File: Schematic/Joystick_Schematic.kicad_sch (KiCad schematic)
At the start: 4 parts

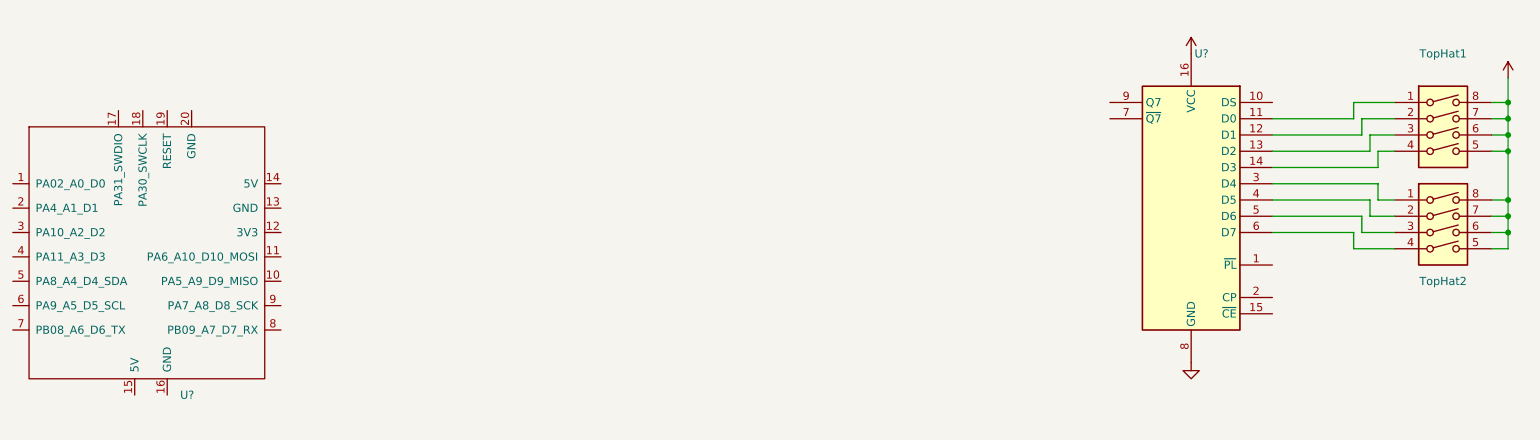
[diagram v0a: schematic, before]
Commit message: removed out of date files and created prove of concept piso code
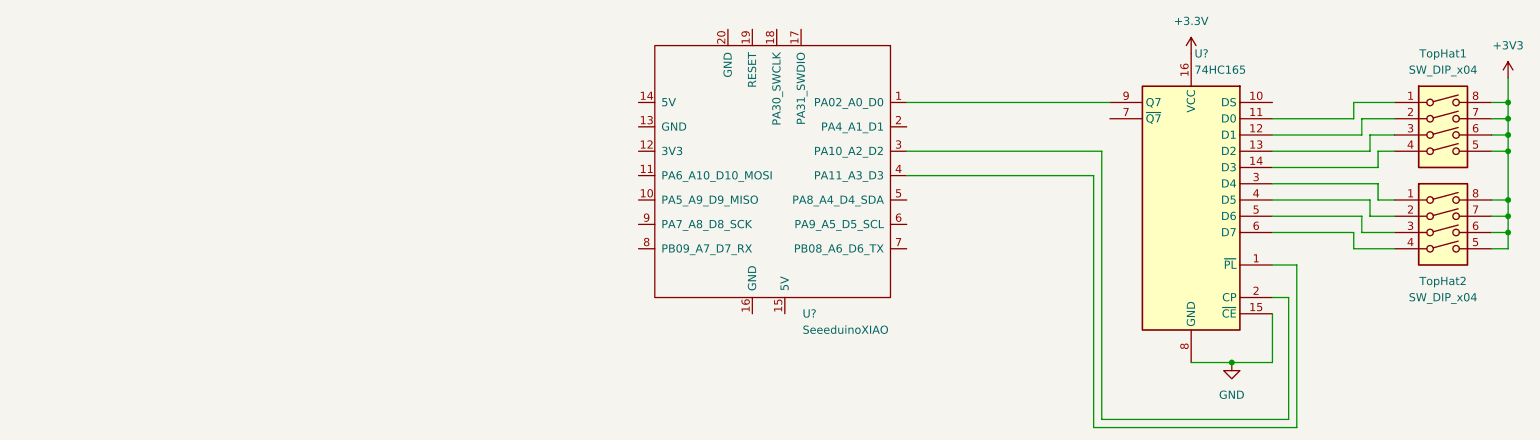
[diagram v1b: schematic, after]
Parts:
- TopHat1, TopHat2: value (none) -> SW_DIP_x04
- U?: value (none) -> SeeeduinoXIAO
- U?: value (none) -> 74HC165
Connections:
- net GND: now also U?.15 (~{CE})
- net at U?.1 (PA02_A0_D0): now also U?.9 (Q7)
- net at U?.3 (PA10_A2_D2): now also U?.2 (CP)
- net at U?.4 (PA11_A3_D3): now also U?.1 (~{PL})
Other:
- moved on the sheet: U?
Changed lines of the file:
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@@
   (junction (at 281.94 40.64) (diameter 0) (color 0 0 0 0)
   )
+  (junction (at 238.76 78.74) (diameter 0) (color 0 0 0 0)
+  )
   (junction (at 281.94 43.18) (diameter 0) (color 0 0 0 0)
   )
+  (wire (pts (xy 217.17 88.9) (xy 217.17 49.53))
+    (stroke (width 0) (type default) (color 0 0 0 0))
+  )
   (wire (pts (xy 257.81 38.1) (xy 257.81 40.64))
     (stroke (width 0) (type default) (color 0 0 0 0))
   )
+  (wire (pts (xy 248.92 63.5) (xy 245.11 63.5))
+    (stroke (width 0) (type default) (color 0 0 0 0))
+  )
   (wire (pts (xy 279.4 43.18) (xy 281.94 43.18))
     (stroke (width 0) (type default) (color 0 0 0 0))
@@
     (stroke (width 0) (type default) (color 0 0 0 0))
   )
+  (wire (pts (xy 247.65 68.58) (xy 247.65 87.63))
+    (stroke (width 0) (type default) (color 0 0 0 0))
+  )
+  (wire (pts (xy 217.17 88.9) (xy 248.92 88.9))
+    (stroke (width 0) (type default) (color 0 0 0 0))
+  )
+  (wire (pts (xy 245.11 78.74) (xy 245.11 71.12))
+    (stroke (width 0) (type default) (color 0 0 0 0))
+  )
   (wire (pts (xy 281.94 38.1) (xy 279.4 38.1))
     (stroke (width 0) (type default) (color 0 0 0 0))
@@
     (stroke (width 0) (type default) (color 0 0 0 0))
   )
+  (wire (pts (xy 218.44 45.72) (xy 187.96 45.72))
+    (stroke (width 0) (type default) (color 0 0 0 0))
+  )
   (wire (pts (xy 260.35 55.88) (xy 260.35 53.34))
     (stroke (width 0) (type default) (color 0 0 0 0))
@@
     (stroke (width 0) (type default) (color 0 0 0 0))
   )
+  (wire (pts (xy 218.44 87.63) (xy 218.44 45.72))
+    (stroke (width 0) (type default) (color 0 0 0 0))
+  )
   (wire (pts (xy 279.4 58.42) (xy 281.94 58.42))
     (stroke (width 0) (type default) (color 0 0 0 0))
   )
+  (wire (pts (xy 238.76 78.74) (xy 245.11 78.74))
+    (stroke (width 0) (type default) (color 0 0 0 0))
+  )
+  (wire (pts (xy 245.11 68.58) (xy 247.65 68.58))
+    (stroke (width 0) (type default) (color 0 0 0 0))
+  )
   (wire (pts (xy 259.08 40.64) (xy 259.08 43.18))
     (stroke (width 0) (type default) (color 0 0 0 0))
@@
     (stroke (width 0) (type default) (color 0 0 0 0))
   )
+  (wire (pts (xy 217.17 49.53) (xy 187.96 49.53))
+    (stroke (width 0) (type default) (color 0 0 0 0))
+  )
   (wire (pts (xy 257.81 60.96) (xy 257.81 58.42))
     (stroke (width 0) (type default) (color 0 0 0 0))
@@
     (stroke (width 0) (type default) (color 0 0 0 0))
   )
+  (wire (pts (xy 187.96 38.1) (xy 219.71 38.1))
+    (stroke (width 0) (type default) (color 0 0 0 0))
+  )
   (wire (pts (xy 259.08 55.88) (xy 259.08 58.42))
     (stroke (width 0) (type default) (color 0 0 0 0))
@@
     (stroke (width 0) (type default) (color 0 0 0 0))
   )
+  (wire (pts (xy 247.65 87.63) (xy 218.44 87.63))
+    (stroke (width 0) (type default) (color 0 0 0 0))
+  )
   (wire (pts (xy 261.62 45.72) (xy 261.62 48.26))
     (stroke (width 0) (type default) (color 0 0 0 0))
@@
     (stroke (width 0) (type default) (color 0 0 0 0))
   )
+  (wire (pts (xy 248.92 88.9) (xy 248.92 63.5))
+    (stroke (width 0) (type default) (color 0 0 0 0))
+  )
   (wire (pts (xy 279.4 40.64) (xy 281.94 40.64))
     (stroke (width 0) (type default) (color 0 0 0 0))
@@
     (stroke (width 0) (type default) (color 0 0 0 0))
   )
+  (wire (pts (xy 238.76 78.74) (xy 232.41 78.74))
+    (stroke (width 0) (type default) (color 0 0 0 0))
+  )
   (wire (pts (xy 279.4 60.96) (xy 281.94 60.96))
     (stroke (width 0) (type default) (color 0 0 0 0))
@@
     (stroke (width 0) (type default) (color 0 0 0 0))
   )
-  (symbol (lib_id "power:GND") (at 232.41 78.74 0) (unit 1)
-    (in_bom yes) (on_board yes) (fields_autoplaced)
-    (property "Reference" "#PWR?" (id 0) (at 232.41 85.09 0)
-      (effects (font (size 1.27 1.27)) hide)
-    )
-    (property "Value" "" (id 1) (at 232.41 83.82 0))
-    (property "Footprint" "" (id 2) (at 232.41 78.74 0)
-      (effects (font (size 1.27 1.27)) hide)
-    )
-    (property "Datasheet" "" (id 3) (at 232.41 78.74 0)
-      (effects (font (size 1.27 1.27)) hide)
-    )
-    (pin "1")
-  )
-  (symbol (lib_id "Seeeduino XIAO:SeeeduinoXIAO") (at 69.85 62.23 0) (unit 1)
-    (in_bom yes) (on_board yes) (fields_autoplaced)
-    (property "Reference" "U?" (id 0) (at 74.4094 83.82 0)
-      (effects (font (size 1.27 1.27)) (justify left))
-    )
-    (property "Value" "" (id 1) (at 74.4094 86.36 0)
-      (effects (font (size 1.27 1.27)) (justify left))
-    )
-    (property "Footprint" "" (id 2) (at 60.96 57.15 0)
-      (effects (font (size 1.27 1.27)) hide)
-    )
-    (property "Datasheet" "" (id 3) (at 60.96 57.15 0)
+  (symbol (lib_id "power:GND") (at 238.76 78.74 0) (unit 1)
+    (in_bom yes) (on_board yes) (fields_autoplaced)
+    (property "Reference" "#PWR?" (id 0) (at 238.76 85.09 0)
+      (effects (font (size 1.27 1.27)) hide)
+    )
+    (property "Value" "GND" (id 1) (at 238.76 83.82 0))
+    (property "Footprint" "" (id 2) (at 238.76 78.74 0)
+      (effects (font (size 1.27 1.27)) hide)
+    )
+    (property "Datasheet" "" (id 3) (at 238.76 78.74 0)
+      (effects (font (size 1.27 1.27)) hide)
+    )
+    (pin "1")
+  )
+  (symbol (lib_id "Seeeduino XIAO:SeeeduinoXIAO") (at 166.37 49.53 0) (mirror y) (unit 1)
+    (in_bom yes) (on_board yes) (fields_autoplaced)
+    (property "Reference" "U?" (id 0) (at 171.6787 71.12 0)
+      (effects (font (size 1.27 1.27)) (justify right))
+    )
+    (property "Value" "SeeeduinoXIAO" (id 1) (at 171.6787 73.66 0)
+      (effects (font (size 1.27 1.27)) (justify right))
+    )
+    (property "Footprint" "" (id 2) (at 175.26 44.45 0)
+      (effects (font (size 1.27 1.27)) hide)
+    )
+    (property "Datasheet" "" (id 3) (at 175.26 44.45 0)
       (effects (font (size 1.27 1.27)) hide)
     )
@@
     (in_bom yes) (on_board yes) (fields_autoplaced)
     (property "Reference" "TopHat2" (id 0) (at 271.78 66.04 0))
-    (property "Value" "" (id 1) (at 271.78 68.58 0))
+    (property "Value" "SW_DIP_x04" (id 1) (at 271.78 68.58 0))
     (property "Footprint" "" (id 2) (at 271.78 58.42 0)
       (effects (font (size 1.27 1.27)) hide)
@@
       (effects (font (size 1.27 1.27)) hide)
     )
-    (property "Value" "" (id 1) (at 232.41 25.4 0))
+    (property "Value" "+3.3V" (id 1) (at 232.41 25.4 0))
     (property "Footprint" "" (id 2) (at 232.41 30.48 0)
       (effects (font (size 1.27 1.27)) hide)
@@
       (effects (font (size 1.27 1.27)) hide)
     )
-    (property "Value" "" (id 1) (at 281.94 29.21 0))
+    (property "Value" "+3V3" (id 1) (at 281.94 29.21 0))
     (property "Footprint" "" (id 2) (at 281.94 34.29 0)
       (effects (font (size 1.27 1.27)) hide)
@@
       (effects (font (size 1.27 1.27)) (justify right))
     )
-    (property "Value" "" (id 1) (at 232.9306 33.02 0)
+    (property "Value" "74HC165" (id 1) (at 232.9306 33.02 0)
       (effects (font (size 1.27 1.27)) (justify right))
     )
@@
     (in_bom yes) (on_board yes) (fields_autoplaced)
     (property "Reference" "TopHat1" (id 0) (at 271.78 30.48 0))
-    (property "Value" "" (id 1) (at 271.78 33.02 0))
+    (property "Value" "SW_DIP_x04" (id 1) (at 271.78 33.02 0))
     (property "Footprint" "" (id 2) (at 271.78 43.18 0)
       (effects (font (size 1.27 1.27)) hide)

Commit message: continued schematic
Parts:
- added R1, R2: 1k, symbol Device:R
- added RN1, RN2, RN3: 1k, Resistor_THT:R_Array_SIP9, symbol Device:R_Network08
- added RV? (x2): (no value), symbol Device:R_Potentiometer
- added Switches (x2): SW_DIP_x04, symbol Switch:SW_DIP_x04
- added U? (x2): 74HC165, symbol 74xx:74HC165
- U?: footprint (none) -> Seeeduino XIAO KICAD:Seeeduino XIAO-MOUDLE14P-2.54-21X17.8MM
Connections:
- net +3V3: now also U?.12 (3V3), R1.1, R2.1, Switches.5, Switches.5, Switches.6, Switches.6, Switches.7, Switches.7, Switches.8, Switches.8, U?.16 (VCC), U?.16 (VCC)
- net GND: now also U?.10 (DS), RN1.1 (common), RN2.1 (common), RN3.1 (common), U?.10 (DS), U?.10 (DS), U?.15 (~{CE}), U?.15 (~{CE}), U?.8 (GND), U?.8 (GND)
- net RKJXT1F/Encoder A: now reaches U?.10 (PA5_A9_D9_MISO)
- net RKJXT1F/Encoder A: now also R2.2
- net at U?.11 (PA6_A10_D10_MOSI): now also U?.9 (Q7)
- net at U?.2 (PA4_A1_D1): now also U?.9 (Q7)
- net at U?.2 (CP), U?.3 (PA10_A2_D2): now also U?.2 (CP)
- net at U?.1 (~{PL}), U?.4 (PA11_A3_D3): now also U?.1 (~{PL})
- net RKJXT1F/Encoder B: now reaches U?.9 (PA7_A8_D8_SCK)
- net RKJXT1F/Encoder B: now also R1.2
- net at TopHat2.1, U?.3 (D4): now also RN1.6 (R5)
- net at TopHat2.2, U?.4 (D5): now also RN1.7 (R6)
- net at TopHat2.3, U?.5 (D6): now also RN1.8 (R7)
- net at TopHat2.4, U?.6 (D7): now also RN1.9 (R8)
- net at TopHat1.1, U?.11 (D0): now also RN1.2 (R1)
- net at TopHat1.2, U?.12 (D1): now also RN1.3 (R2)
- net at TopHat1.3, U?.13 (D2): now also RN1.4 (R3)
- net at TopHat1.4, U?.14 (D3): now also RN1.5 (R4)
- new net: RN2.2 (R1), Switches.1, U?.11 (D0)
- new net: RN2.3 (R2), Switches.2, U?.12 (D1)
- new net: RN2.4 (R3), Switches.3, U?.13 (D2)
- new net: RN2.5 (R4), Switches.4, U?.14 (D3)
- new net: RN2.6 (R5), Switches.1, U?.3 (D4)
- new net: RN2.7 (R6), Switches.2, U?.4 (D5)
- new net: RN2.8 (R7), Switches.3, U?.5 (D6)
- new net: RN2.9 (R8), Switches.4, U?.6 (D7)
- new net RKJXT1F/Push A: RN3.6 (R5), U?.3 (D4)
- new net RKJXT1F/Push B: RN3.5 (R4), U?.14 (D3)
- new net RKJXT1F/Push C: RN3.4 (R3), U?.13 (D2)
- new net RKJXT1F/Push Center: RN3.2 (R1), U?.11 (D0)
- new net RKJXT1F/Push D: RN3.3 (R2), U?.12 (D1)
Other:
- added sheet RKJXT1F (rkjxt1f.kicad_sch)
- moved on the sheet: TopHat1, TopHat2, U?

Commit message: Schematic update
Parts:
- removed Switches (x2), TopHat1, TopHat2: SW_DIP_x04, symbol Switch:SW_DIP_x04
- removed U?: 74HC165, symbol 74xx:74HC165
- added SW1: RKJXT1F42001, symbol Alps-RKJXT1F:RKJXT1F42001
- added SW2, SW3, SW4, SW5: SKQUCAA010, Alps-SKQU:SKQUCAA010, symbol Alps-SKQU:SKQUCAA010
- added U4: (no value), symbol 74xx:74HC165
- R1, R2: value 1k -> (none)
- RV1, RV2: renamed from RV?; value (none) -> R_Potentiometer
- U1, U3: renamed from U?; value 74HC165 -> (none)
- gave numbers to parts that had none: 1
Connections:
- net +3V3: now also RV1.3, RV2.3, SW1. (Up), SW2.4 (Com), SW3.4 (Com), SW4.4 (Com), SW5.4 (Com), U4.16 (VCC)
- net GND: now also SW1. (Up), U4.10 (DS), U4.15 (~{CE}), U4.8 (GND)
- net at U2.2 (PA4_A1_D1): now also U4.9 (Q7)
- net at U2.3 (PA10_A2_D2), U3.2 (CP): now also U1.2 (CP), U4.2 (CP)
- net at U2.4 (PA11_A3_D3), U3.1 (~{PL}): now also U1.1 (~{PL}), U4.1 (~{PL})
- net at U2.7 (PB08_A6_D6_TX): now also RV2.1
- net at U2.8 (PB09_A7_D7_RX): now also RV1.1
- net at RN1.2 (R1), U3.11 (D0): now also SW2.5 (D_Right)
- net at RN1.3 (R2), U3.12 (D1): now also SW2.3 (C_Down)
- net at RN1.4 (R3), U3.13 (D2): now also SW2.2 (B_Left)
- net at RN1.5 (R4), U3.14 (D3): now also SW2.1 (A_Up)
- net at RN1.6 (R5), U3.3 (D4): now also SW3.5 (D_Right)
- net at RN1.7 (R6), U3.4 (D5): now also SW3.3 (C_Down)
- net at RN1.8 (R7), U3.5 (D6): now also SW3.2 (B_Left)
- net at RN1.9 (R8), U3.6 (D7): now also SW3.1 (A_Up)
- net at RN2.2 (R1): now also SW4.5 (D_Right), U4.11 (D0)
- net at RN2.3 (R2): now also SW4.3 (C_Down), U4.12 (D1)
- net at RN2.4 (R3): now also SW4.2 (B_Left), U4.13 (D2)
- net at RN2.5 (R4): now also SW4.1 (A_Up), U4.14 (D3)
- net at RN2.6 (R5): now also SW5.5 (D_Right), U4.3 (D4)
- net at RN2.7 (R6): now also SW5.3 (C_Down), U4.4 (D5)
- net at RN2.8 (R7): now also SW5.2 (B_Left), U4.5 (D6)
- net at RN2.9 (R8): now also SW5.1 (A_Up), U4.6 (D7)
- net RKJXT1F/Encoder A: no longer names the net of R2.2, U2.10 (PA5_A9_D9_MISO)
- net RKJXT1F/Encoder A: now also SW1. (Up)
- net RKJXT1F/Encoder B: no longer names the net of R1.2, U2.9 (PA7_A8_D8_SCK)
- net RKJXT1F/Encoder B: now also SW1. (Up)
- net RKJXT1F/Push A: no longer names the net of RN3.6 (R5), U1.3 (D4)
- net RKJXT1F/Push A: now also SW1. (Up)
- net RKJXT1F/Push B: no longer names the net of RN3.5 (R4), U1.14 (D3)
- net RKJXT1F/Push B: now also SW1. (Up)
- net RKJXT1F/Push C: no longer names the net of RN3.4 (R3), U1.13 (D2)
- net RKJXT1F/Push C: now also SW1. (Up)
- net RKJXT1F/Push Center: no longer names the net of RN3.2 (R1), U1.11 (D0)
- net RKJXT1F/Push Center: now also SW1. (Up)
- net RKJXT1F/Push D: no longer names the net of RN3.3 (R2), U1.12 (D1)
- net RKJXT1F/Push D: now also SW1. (Up)
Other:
- removed sheet RKJXT1F
- moved on the sheet: RV1, RV2

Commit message: Schematic update again and started PCB
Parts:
- removed RN1, RN2, RN3: 1k, Resistor_THT:R_Array_SIP9, symbol Device:R_Network08
- removed RV1, RV2: R_Potentiometer, symbol Device:R_Potentiometer
- removed SW4, SW5: SKQUCAA010, Alps-SKQU:SKQUCAA010, symbol Alps-SKQU:SKQUCAA010
- removed U2: SeeeduinoXIAO, Seeeduino XIAO KICAD:Seeeduino XIAO-MOUDLE14P-2.54-21X17.8MM, symbol Seeeduino XIAO:SeeeduinoXIAO
- added C1, C4: 100nF, Resistor_SMD:R_0201_0603Metric_Pad0.64x0.40mm_HandSolder, symbol Device:C
- added J1: (no value), symbol Connector:Conn_01x06_Female
- added J2: (no value), symbol Connector:Conn_01x04_Female
- added J3: (no value), symbol Connector:Conn_01x02_Female
- added JUSB1: USB_B_Micro, Connector_USB:USB_Micro-B_Molex_47346-0001, symbol Connector:USB_B_Micro
- added RN1, RN2, RN3, RN4, RN5, RN6: (no value), symbol Device:R_Network04
- added RP1A1, RP1B1: 1k, Resistor_SMD:R_0201_0603Metric_Pad0.64x0.40mm_HandSolder, symbol Device:R
- added RV1: (no value), symbol Alps-RKJXV:RKJXV122400R
- added U2: ATmega328P-A, Package_QFP:TQFP-32_7x7mm_P0.8mm, symbol MCU_Microchip_ATmega:ATmega328P-A
- added U5: CH340G, Package_SO:SOIC-16_3.9x9.9mm_P1.27mm, symbol Interface_USB:CH340G
- R1, R2: value (none) -> 1k; footprint (none) -> Resistor_SMD:R_0201_0603Metric_Pad0.64x0.40mm_HandSolder
- SW1: value RKJXT1F42001 -> (none)
- U1, U3, U4: value (none) -> 74HC165; footprint (none) -> Package_SO:TSSOP-16_4.4x5mm_P0.65mm
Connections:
- net GND: now also C1.2, JUSB1.5 (GND), JUSB1.6 (Shield), RN1.1 (common), RN2.1 (common), RN3.1 (common), RN4.1 (common), RN5.1 (common), RN6.1 (common), RV1.3 (X_GND), RV1.4 (Y_GND), RV1.5 (GND), U2.21 (GND), U2.3 (GND), U2.5 (GND)
- net SH_DATA1: now reaches U3.9 (Q7)
- net SH_DATA1: now also U2.12 (PB0)
- net ENCODER_B: now reaches R2.2, SW1. (Up)
- net ENCODER_B: now also J3.2 (Pin_2), U2.1 (PD3)
- net SH_DATA3: now reaches U1.9 (Q7)
- net SH_DATA3: now also U2.14 (PB2)
- net SH_DATA2: now reaches U4.9 (Q7)
- net SH_DATA2: now also U2.13 (PB1)
- net SH_CLK: now reaches U1.2 (CP), U3.2 (CP), U4.2 (CP)
- net SH_CLK: now also U2.23 (PC0)
- net SH_LATCH: now reaches U1.1 (~{PL}), U3.1 (~{PL}), U4.1 (~{PL})
- net SH_LATCH: now also U2.24 (PC1)
- net ENCODER_A: now reaches R1.2, SW1. (Up)
- net ENCODER_A: now also J3.1 (Pin_1), U2.32 (PD2)
- net at SW2.5 (D_Right), U3.11 (D0): now also RN1.2 (R1)
- net at SW2.3 (C_Down), U3.12 (D1): now also RN1.3 (R2)
- net at SW2.2 (B_Left), U3.13 (D2): now also RN1.4 (R3)
- net at SW2.1 (A_Up), U3.14 (D3): now also RN1.5 (R4)
- net at SW3.5 (D_Right), U3.3 (D4): now also RN2.2 (R1)
- net at SW3.3 (C_Down), U3.4 (D5): now also RN2.3 (R2)
- net at SW3.2 (B_Left), U3.5 (D6): now also RN2.4 (R3)
- net at SW3.1 (A_Up), U3.6 (D7): now also RN2.5 (R4)
- net HAT1_PUSH: now reaches SW2.6 (Center)
- net HAT1_PUSH: now also U4.5 (D6), RN4.4 (R3)
- net HAT2_PUSH: now reaches U4.6 (D7)
- net HAT2_PUSH: now also SW3.6 (Center), RN4.5 (R4)
- net NC: now reaches U4.4 (D5)
- net NC: now also U1.6 (D7), J1.6 (Pin_6), RN4.3 (R2), RN5.2 (R1)
- net TOP_SIDE_PUSH: now reaches U4.3 (D4)
- net TOP_SIDE_PUSH: now also J1.5 (Pin_5), RN4.2 (R1)
- net PANEL_PUSH: now reaches U4.14 (D3)
- net PANEL_PUSH: now also J1.4 (Pin_4), RN3.5 (R4)
- net TRIGGER_2: now reaches U4.13 (D2)
- net TRIGGER_2: now also J1.3 (Pin_3), RN3.4 (R3)
- net TRIGGER_1: now reaches U4.12 (D1)
- net TRIGGER_1: now also J1.2 (Pin_2), RN3.3 (R2)
- net THUMB_PUSH: now reaches U4.11 (D0)
- net THUMB_PUSH: now also J1.1 (Pin_1), RN3.2 (R1), RV1.9 (SW2)
- net at SW1. (Up), U1.11 (D0): now also RN6.5 (R4)
- net at SW1. (Up), U1.12 (D1): now also RN6.4 (R3)
- net at SW1. (Up), U1.13 (D2): now also RN6.3 (R2)
- net at SW1. (Up), U1.14 (D3): now also RN6.2 (R1)
- net at SW1. (Up), U1.3 (D4): now also RN5.5 (R4)
- net BRAKE: now reaches U1.4 (D5)
- net BRAKE: now also RN5.4 (R3)
- net PINKY_PUSH: now reaches U1.5 (D6)
- net PINKY_PUSH: now also RN5.3 (R2)
- net +3V3 renamed +5V
- net +5V: now also JUSB1.1 (VBUS), RV1.1 (X_VCC), RV1.2 (Y_VCC), RV1.8 (SW1), U2.18 (AVCC), U2.4 (VCC), U2.6 (VCC), U5.16 (VCC)
- new net: RP1B1.1, U2.31 (PD1)
- new net: C1.1, U2.20 (AREF)
- new net: RP1A1.1, U2.30 (PD0)
- new net: C4.1, U5.13 (~{DTR})
- new net: JUSB1.3 (D+), U5.5 (UD+)
- new net: JUSB1.2 (D-), U5.6 (UD-)
- new net RESET: C4.2, U2.29 (~{RESET}/PC6)
- new net RX: RP1A1.2, U5.2 (TXD)
- new net SCL: J2.4 (Pin_4), U2.28 (PC5)
- new net SDA: J2.3 (Pin_3), U2.27 (PC4)
- new net THUMB_X: J2.1 (Pin_1), RV1.7 (X_OUT), U2.25 (PC2)
- new net THUMB_Y: J2.2 (Pin_2), RV1.6 (Y_OUT), U2.26 (PC3)
- new net TX: RP1B1.2, U5.3 (RXD)
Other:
- note added: "USB"
- moved on the sheet: R1, R2, SW1, SW2, SW3, U1
